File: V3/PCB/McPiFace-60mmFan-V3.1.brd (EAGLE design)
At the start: 88 x 88 mm, 33 parts, among them J2 Fan, J3 DNP, J4 I2C, Q1 SI2307CDS, Q2 2N7002, U1 Tiny85-20-SMT, U3 LIS3DH

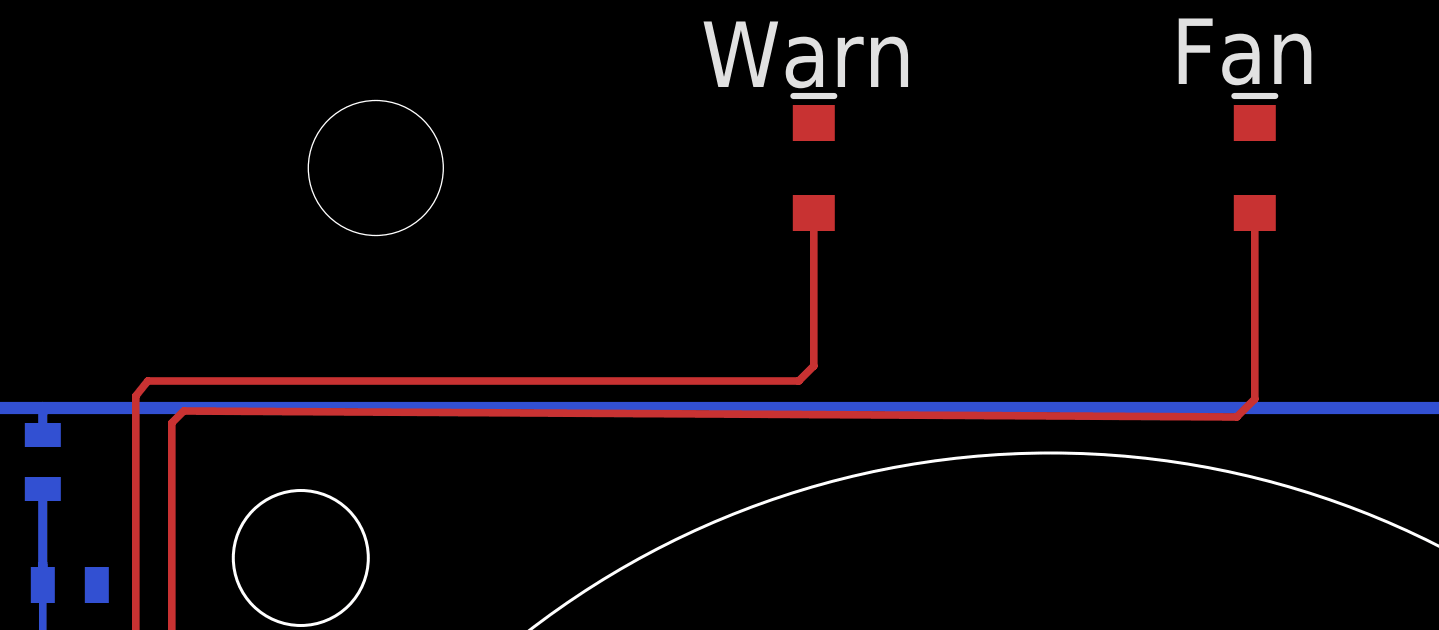
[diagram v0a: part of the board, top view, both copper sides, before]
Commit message: Modified V3 to include some package details.
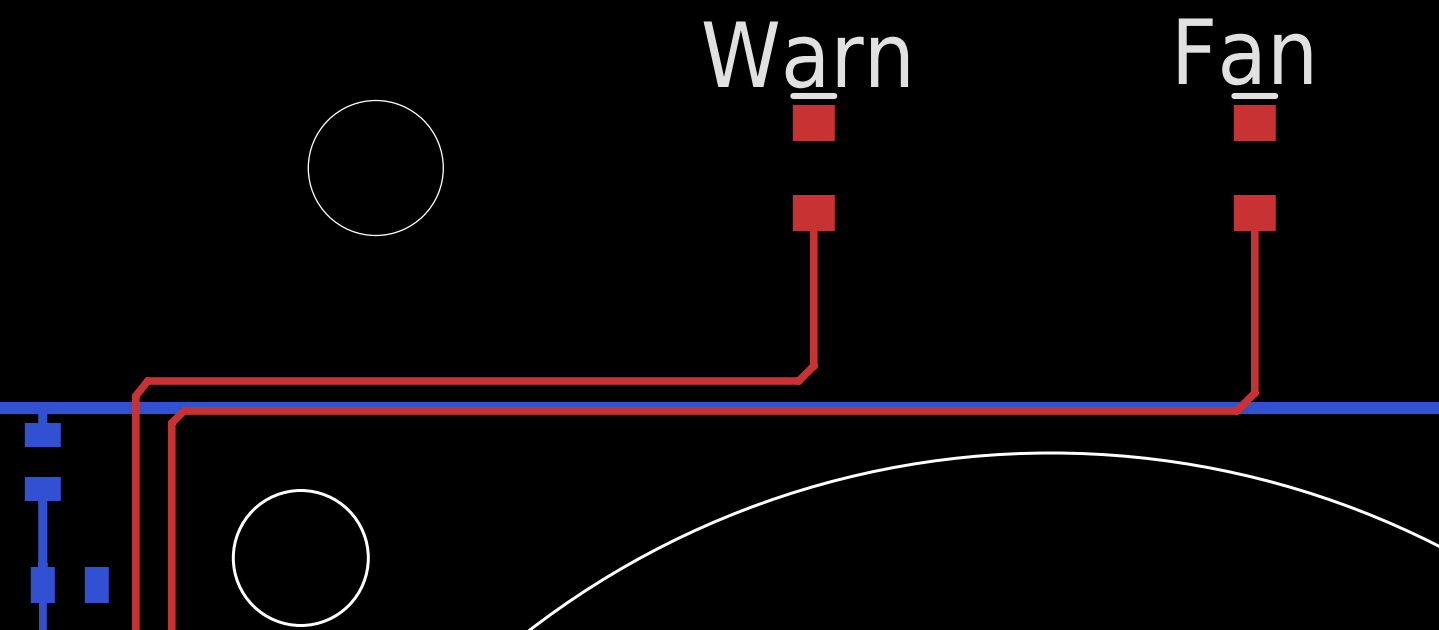
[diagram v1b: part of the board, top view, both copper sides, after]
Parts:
- D1: value IN4148W -> IN4148WS
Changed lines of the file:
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@@
 <text x="77.47" y="29.735" size="1.27" layer="26" ratio="15" rot="MR270">GND</text>
 <text x="32.835" y="84.7" size="2.1844" layer="25" ratio="15">Warn</text>
-<text x="65.3" y="74.1" size="1.778" layer="26" ratio="15" rot="MR0">http://github.com/McPiFace/Fan</text>
+<text x="66.2" y="76.2" size="1.778" layer="26" ratio="15" rot="MR0">http://github.com/McPiFace/Fan</text>
 <text x="10.3" y="5.2" size="1.778" layer="26" ratio="15" rot="MR0">V3.1</text>
 <text x="52" y="4" size="1.778" layer="26" ratio="15" rot="MR0">S.Harrison
@@
 <attribute name="NAME" x="82.651" y="24.9" size="0.6096" layer="26" font="vector" ratio="20" rot="MR90" align="bottom-center"/>
 <attribute name="FARNELL" value="1779262" x="81" y="24.9" size="1.778" layer="28" rot="MR0" display="off"/>
+<attribute name="LCSC" value="C189813" x="81" y="24.9" size="1.778" layer="28" rot="MR0" display="off"/>
 </element>
 <element name="Q2" library="SparkFun-DiscreteSemi" package="SOT23-3" value="2N7002" x="81.265" y="20" smashed="yes" rot="MR0">
@@
 <element name="U2" library="SparkFun-IC-Power" package="SOT223" value="" x="3.6" y="64.4" rot="MR180">
 <attribute name="PROD_ID" value="VREG-08170" x="3.6" y="64.4" size="1.778" layer="28" rot="MR180" display="off"/>
+<attribute name="LCSC" value="C126027" x="3.6" y="64.4" size="1.778" layer="28" rot="MR180" display="off"/>
 </element>
 <element name="C1" library="ThingySticks" package="0805" value="0.1uF" x="2.7" y="74" smashed="yes" rot="MR0">
@@
 <attribute name="VALUE" x="3" y="69.489" size="0.6096" layer="28" font="vector" ratio="20" rot="MR180" align="top-center"/>
 </element>
-<element name="D1" library="SparkFun-DiscreteSemi" package="SOD-323" value="IN4148W" x="84.8" y="24.9" smashed="yes" rot="MR270">
+<element name="D1" library="SparkFun-DiscreteSemi" package="SOD-323" value="IN4148WS" x="84.8" y="24.9" smashed="yes" rot="MR270">
 <attribute name="PROD_ID" value="DIO-09646" x="84.8" y="24.9" size="1.778" layer="28" ratio="15" rot="MR270" display="off"/>
 <attribute name="NAME" x="84.7" y="27.538" size="0.6096" layer="26" font="vector" ratio="20" rot="MR180" align="bottom-center"/>
+<attribute name="LCSC" value="C2128" x="84.8" y="24.9" size="1.778" layer="28" rot="MR270" display="off"/>
 </element>
 <element name="D2" library="SparkFun-DiscreteSemi" package="SOD-323" value="15V" x="11.6" y="41.1" rot="MR0">
@@
 <wire x1="15.2" y1="50.3" x2="15.2" y2="73.5" width="0.254" layer="1"/>
 <wire x1="15.2" y1="73.5" x2="15.6" y2="73.9" width="0.254" layer="1"/>
-<wire x1="15.6" y1="73.9" x2="50.7" y2="73.7" width="0.254" layer="1"/>
-<wire x1="50.7" y1="73.7" x2="51.3" y2="74.3" width="0.254" layer="1"/>
-<wire x1="51.3" y1="74.3" x2="51.3" y2="80.5" width="0.254" layer="1"/>
+<wire x1="15.6" y1="73.9" x2="50.7" y2="73.9" width="0.254" layer="1"/>
+<wire x1="50.7" y1="73.9" x2="51.3" y2="74.5" width="0.254" layer="1"/>
+<wire x1="51.3" y1="74.5" x2="51.3" y2="80.5" width="0.254" layer="1"/>
 </signal>
 <signal name="N$4">
